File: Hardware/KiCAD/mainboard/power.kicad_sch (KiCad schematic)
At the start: 48 parts, among them U3 TP6841S6, U4 TPS73233

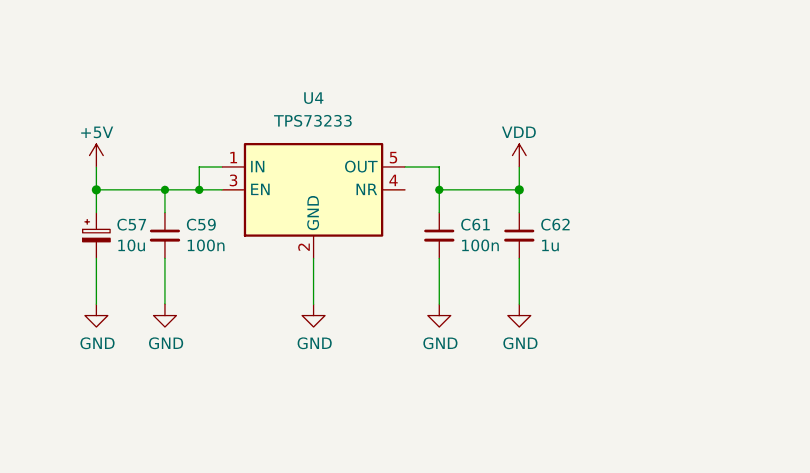
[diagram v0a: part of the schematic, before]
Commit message: J3 UART conn change
Fixes #33
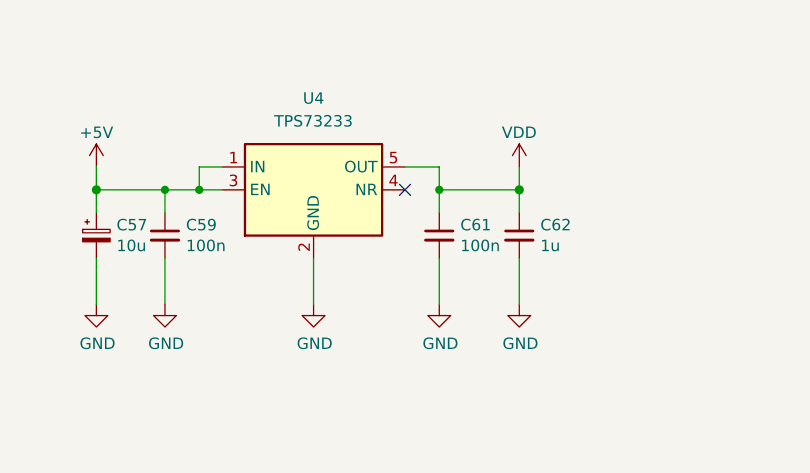
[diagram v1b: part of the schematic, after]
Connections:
- no-connect marks 0 -> 1
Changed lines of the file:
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@@
   (junction (at 87.63 35.56) (diameter 0) (color 0 0 0 0)
   )
+  (no_connect (at 201.93 35.56))
   (wire (pts (xy 137.16 35.56) (xy 137.16 24.13))
     (stroke (width 0) (type default) (color 0 0 0 0))

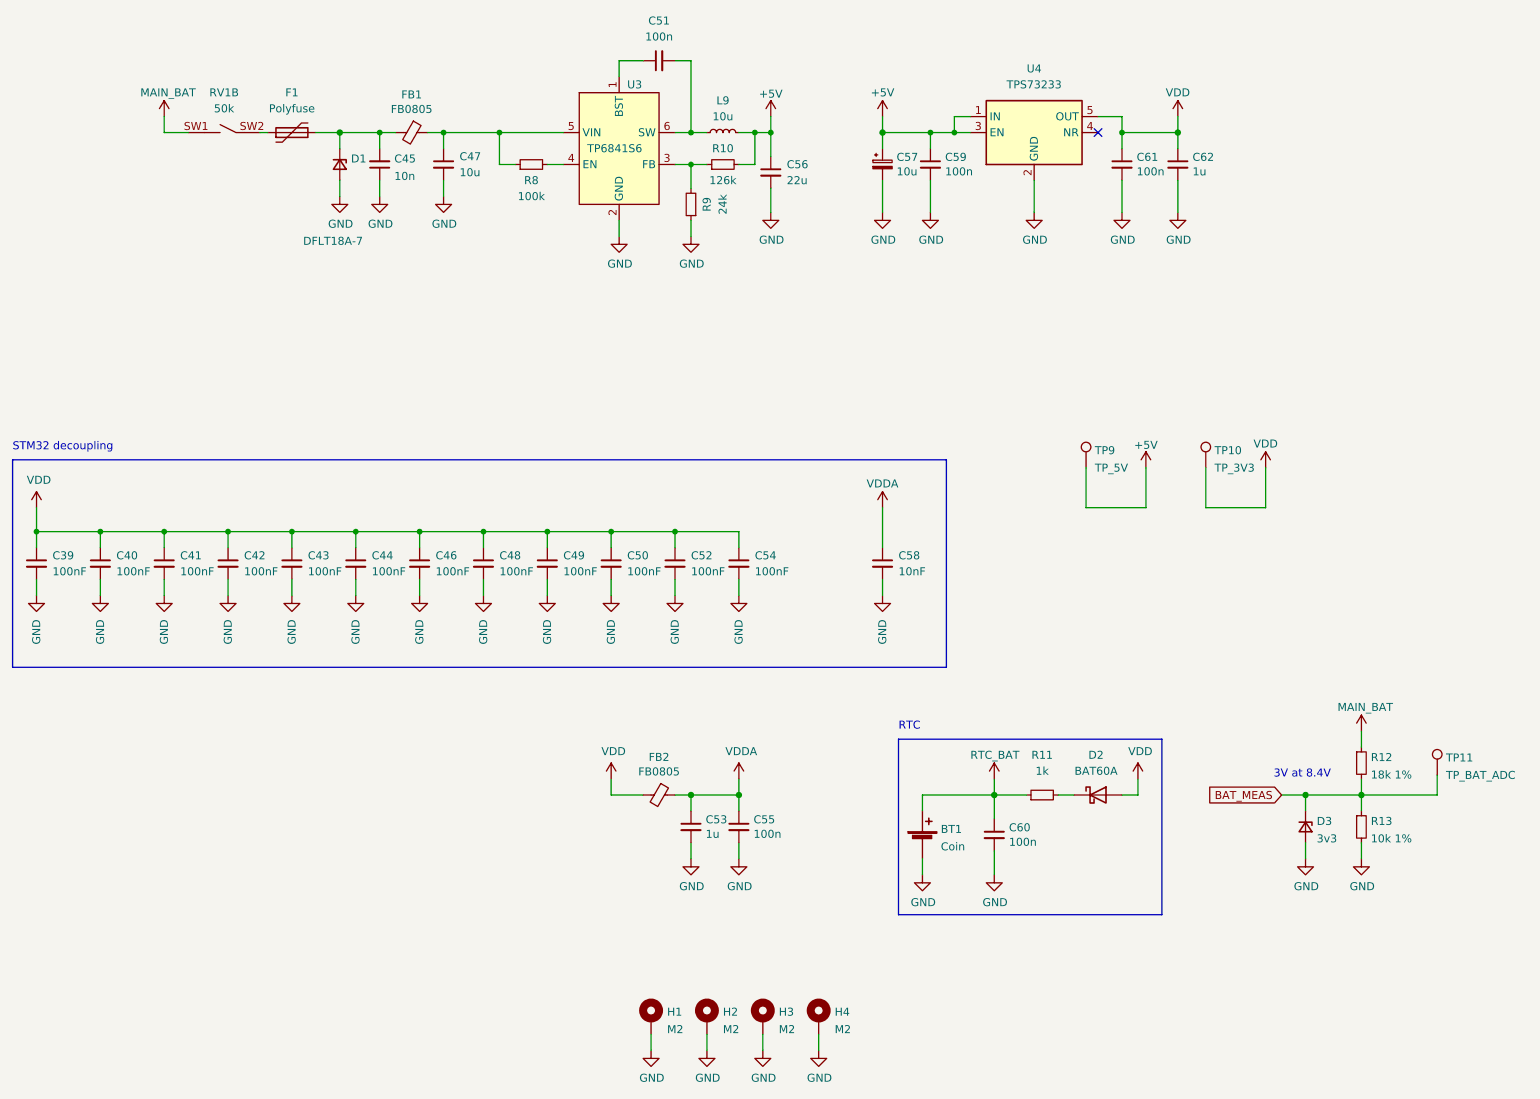
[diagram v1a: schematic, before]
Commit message: MCU swap
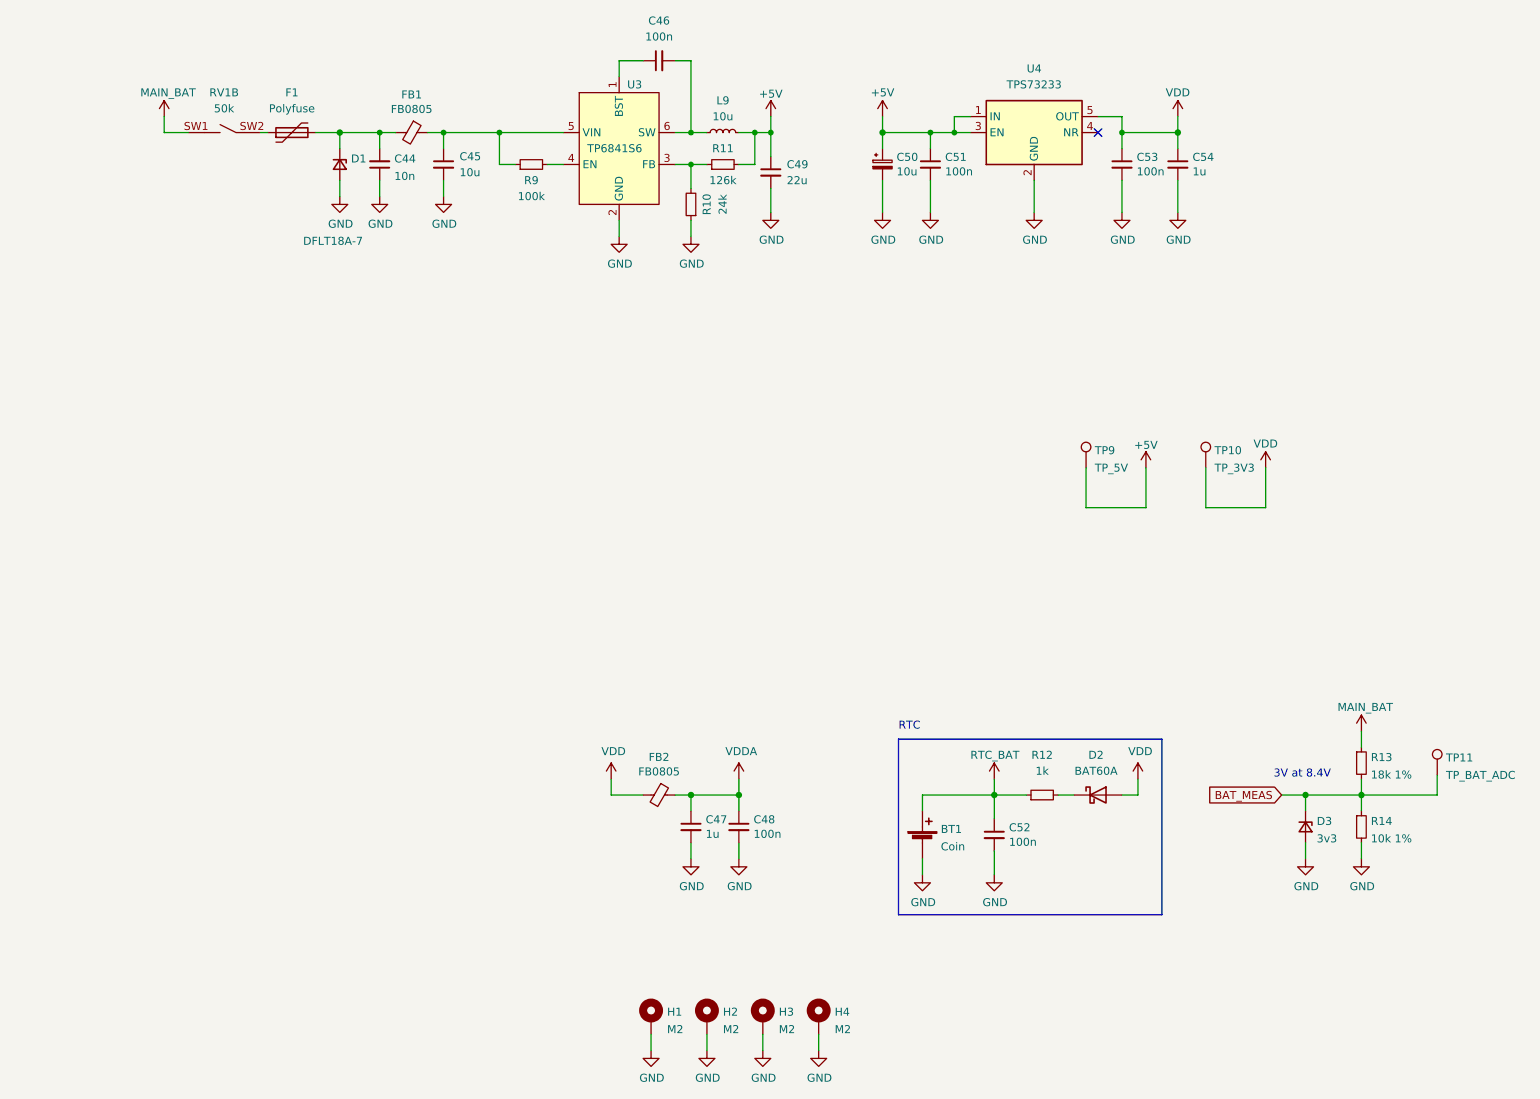
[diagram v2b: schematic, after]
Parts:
- removed C39, C40, C41, C42, C43, C44, C46, C48, C49, C50, C52, C54: 100nF, Capacitor_SMD:C_0402_1005Metric, symbol Device:C_Small
- removed C58: 10nF, Capacitor_SMD:C_0402_1005Metric, symbol Device:C_Small
- renumbered C45 to C44, C47 to C45, C51 to C46, C53 to C47, C55 to C48, C56 to C49, C57 to C50, C59 to C51, C60 to C52, C61 to C53, C62 to C54, R9 to R10, R10 to R11, R11 to R12, R12 to R13, R13 to R14, R8 to R9
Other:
- note removed: "STM32 decoupling"

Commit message: Removed RTC
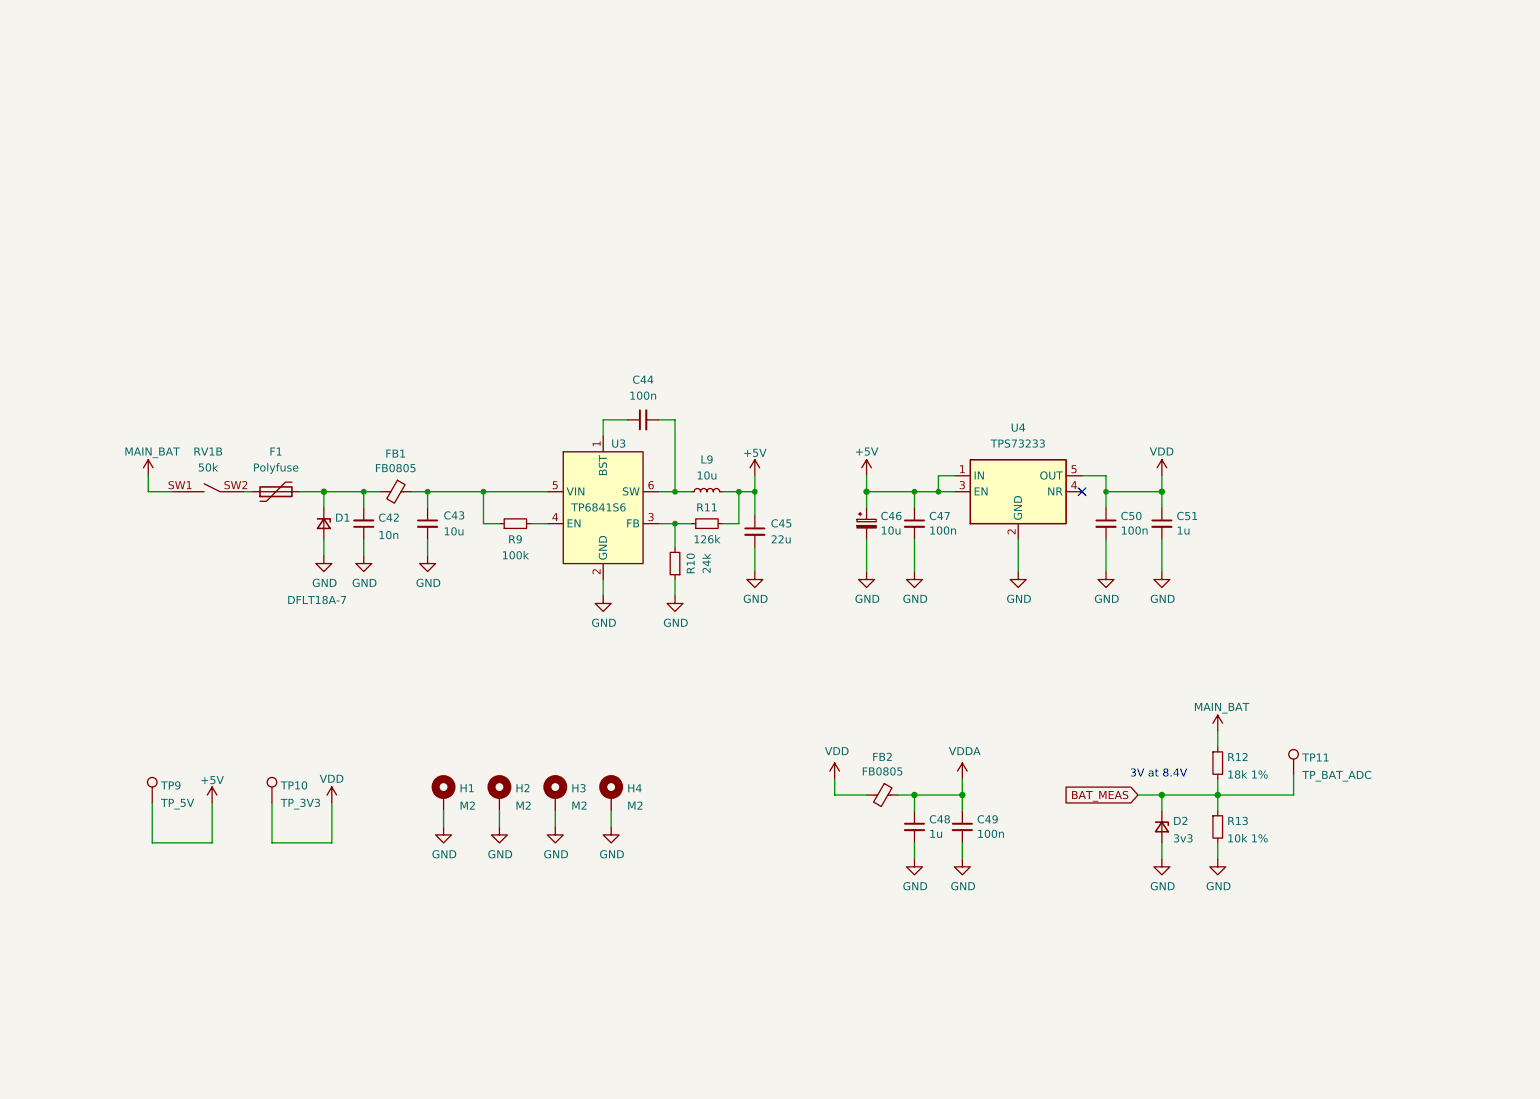
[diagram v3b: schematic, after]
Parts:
- removed BT1: Coin, Battery:BatteryHolder_Keystone_3000_1x12mm, symbol Device:Battery_Cell
- removed C52: 100n, pkl_dipol:C_0603, symbol pkl_device:pkl_C_Small
- removed D2: BAT60A, Diode_SMD:D_SOD-323, symbol Diode:BAT60A
- removed R12: 1k, Resistor_SMD:R_0402_1005Metric, symbol pkl_device:pkl_R_Small
- renumbered C44 to C42, C45 to C43, C46 to C44, C49 to C45, C50 to C46, C51 to C47, C47 to C48, C48 to C49, C53 to C50, C54 to C51, D3 to D2, R13 to R12, R14 to R13
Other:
- note removed: "RTC"
- moved on the sheet: C42, C43, C44, C45, C46, C47, C48, C49, C50, C51, D1, D2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
